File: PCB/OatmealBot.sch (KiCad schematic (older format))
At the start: 7 parts, among them J2 RPi_GPIO

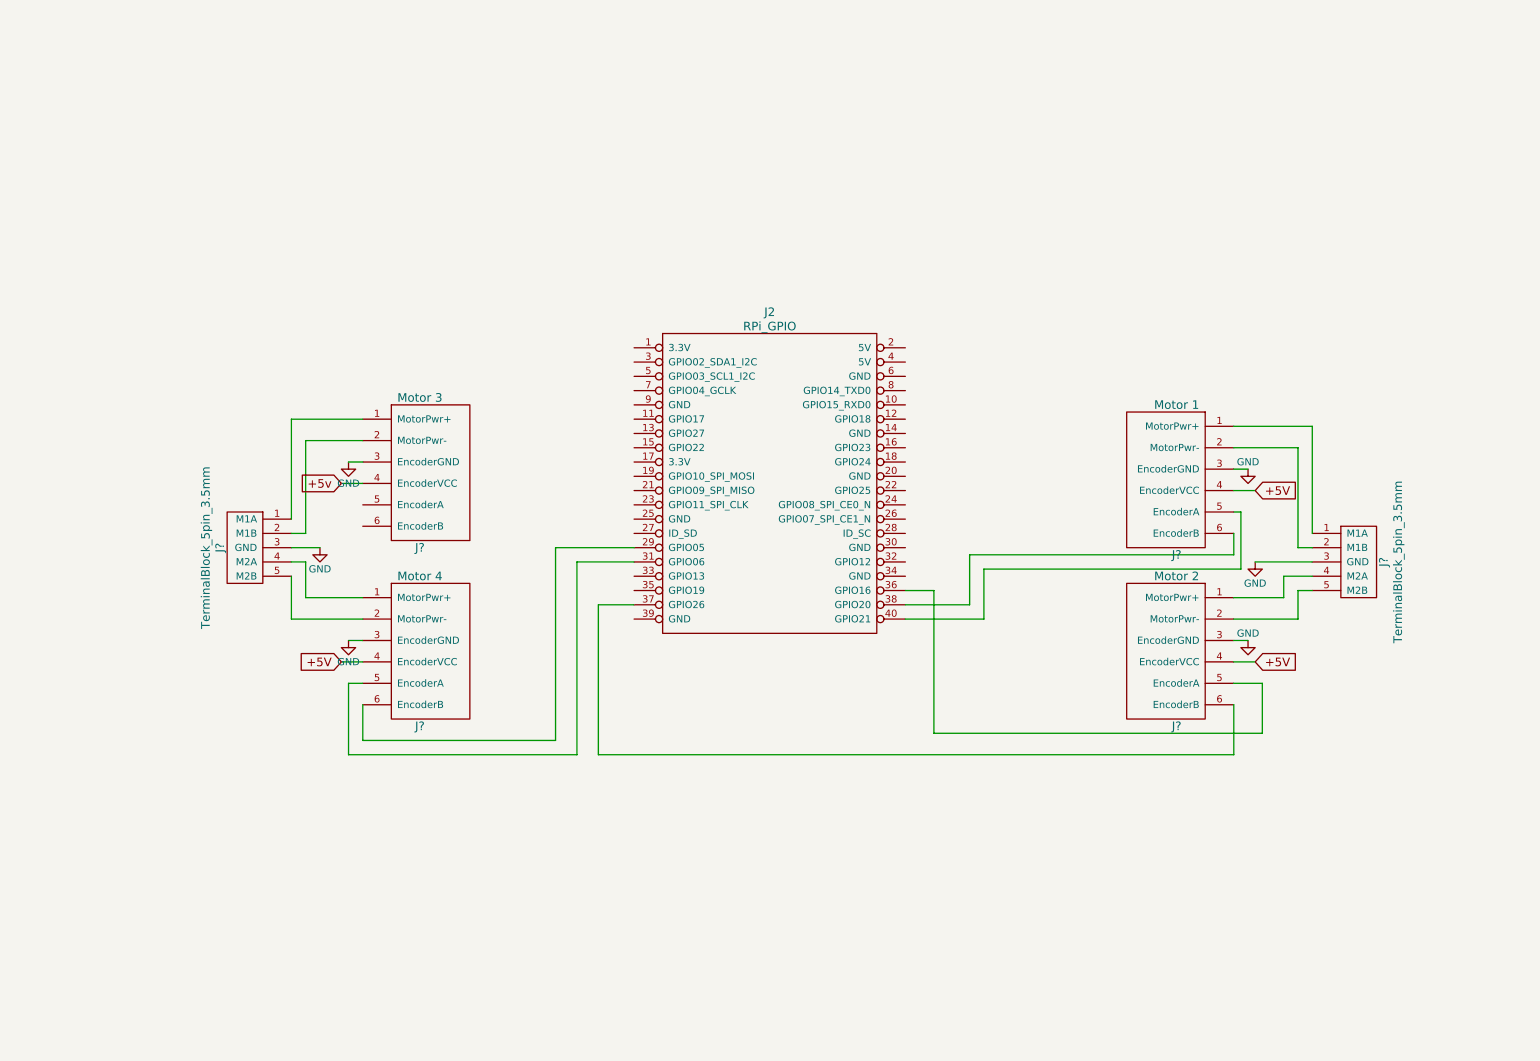
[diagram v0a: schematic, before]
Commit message: Added 5V to 3.3V level shifter on the encoder outputs. Hooked up all encoder outputs.
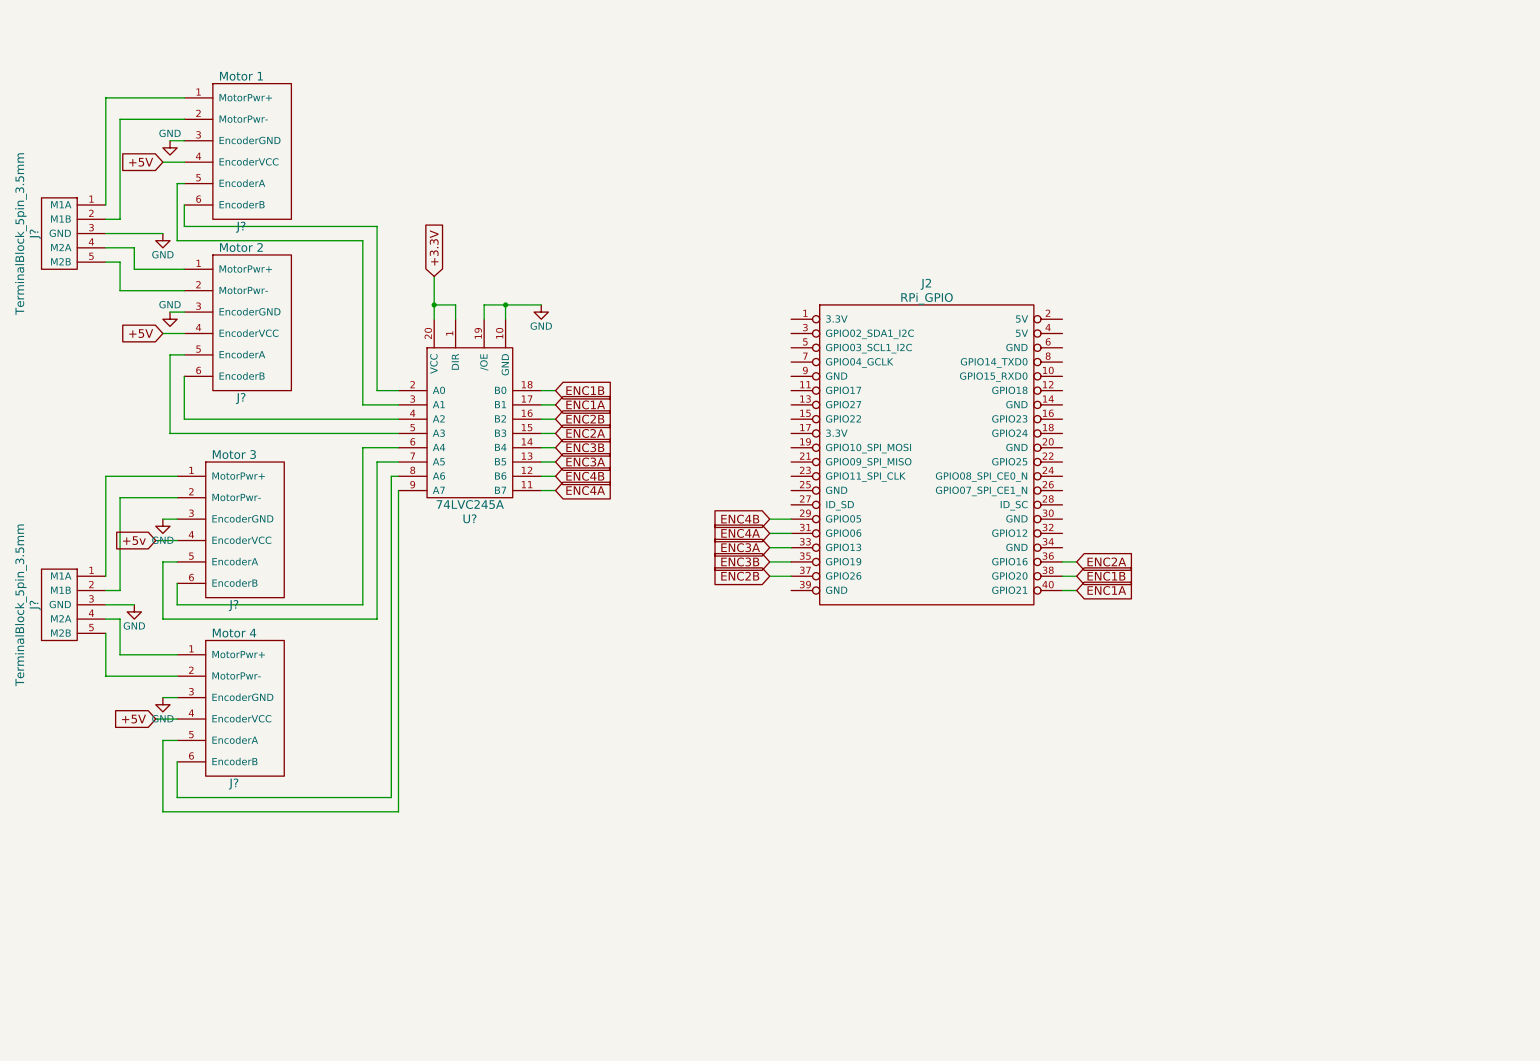
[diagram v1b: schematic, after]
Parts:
- added U?: 74LVC245A, symbol 74LVC245A
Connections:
- net GND: now also U?.10 (GND), U?.19 (/OE)
- net at J?.6 (EncoderB): now also U?.8 (A6); no longer J2.29 (GPIO05)
- net at J?.5 (EncoderA): now also U?.9 (A7); no longer J2.31 (GPIO06)
- net ENC3A: now reaches J2.33 (GPIO13)
- net ENC3A: now also U?.13 (B5)
- net ENC3B: now reaches J2.35 (GPIO19)
- net ENC3B: now also U?.14 (B4)
- net at J?.5 (EncoderA): now also U?.5 (A3); no longer J2.36 (GPIO16)
- net at J?.6 (EncoderB): now also U?.4 (A2); no longer J2.37 (GPIO26)
- net at J?.6 (EncoderB): now also U?.2 (A0); no longer J2.38 (GPIO20)
- net at J?.5 (EncoderA): now also U?.3 (A1); no longer J2.40 (GPIO21)
- net at J?.5 (EncoderA): now also U?.7 (A5)
- net at J?.6 (EncoderB): now also U?.6 (A4)
- new net +3.3V: U?.1 (DIR), U?.20 (VCC)
- new net ENC1A: J2.40 (GPIO21), U?.17 (B1)
- new net ENC1B: J2.38 (GPIO20), U?.18 (B0)
- new net ENC2A: J2.36 (GPIO16), U?.15 (B3)
- new net ENC2B: J2.37 (GPIO26), U?.16 (B2)
- new net ENC4A: J2.31 (GPIO06), U?.11 (B7)
- new net ENC4B: J2.29 (GPIO05), U?.12 (B6)
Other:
- moved on the sheet: J2, J?

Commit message: Added LEDs and servo connectors
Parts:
- added D? (x2): LED, symbol LED
- added J?: ServoHeader1, symbol ServoHeader
- added J?: ServoHeader2, symbol ServoHeader
- added J?: ServoHeader3, symbol ServoHeader
- added R? (x2): 330, symbol R
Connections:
- net +5V: now also J?.2 (Vcc), J?.2 (Vcc), J?.2 (Vcc)
- net GND: now also D?.1 (K), D?.1 (K), J?.1 (GND), J?.1 (GND), J?.1 (GND)
- net at J2.15 (GPIO22): now also R?.1
- net at J2.16 (GPIO23): now also R?.2
- new net: D?.2 (A), R?.1
- new net: D?.2 (A), R?.2
- new net Servo1: J?.3 (Signal)
- new net Servo2: J?.3 (Signal)
- new net Servo3: J?.3 (Signal)
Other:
- note added: "Verify Value"
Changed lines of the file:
@@
 Wire Wire Line
 	7900 4550 8000 4550
+$Comp
+L R R?
+U 1 1 5B24C1E3
+P 8350 3350
+F 0 "R?" V 8430 3350 50  0000 C CNN
+F 1 "330" V 8350 3350 50  0000 C CNN
+F 2 "" V 8280 3350 50  0000 C CNN
+F 3 "" H 8350 3350 50  0000 C CNN
+	1    8350 3350
+	0    1    1    0
+$EndComp
+$Comp
+L R R?
+U 1 1 5B24C256
+P 5700 3350
+F 0 "R?" V 5780 3350 50  0000 C CNN
+F 1 "330" V 5700 3350 50  0000 C CNN
+F 2 "" V 5630 3350 50  0000 C CNN
+F 3 "" H 5700 3350 50  0000 C CNN
+	1    5700 3350
+	0    1    1    0
+$EndComp
+$Comp
+L LED D?
+U 1 1 5B24C2BD
+P 8800 3350
+F 0 "D?" H 8800 3450 50  0000 C CNN
+F 1 "LED" H 8800 3250 50  0000 C CNN
+F 2 "" H 8800 3350 50  0000 C CNN
+F 3 "" H 8800 3350 50  0000 C CNN
+	1    8800 3350
+	-1   0    0    1
+$EndComp
+$Comp
+L LED D?
+U 1 1 5B24C3DB
+P 5250 3350
+F 0 "D?" H 5250 3450 50  0000 C CNN
+F 1 "LED" H 5250 3250 50  0000 C CNN
+F 2 "" H 5250 3350 50  0000 C CNN
+F 3 "" H 5250 3350 50  0000 C CNN
+	1    5250 3350
+	1    0    0    -1
+$EndComp
+$Comp
+L GND #PWR?
+U 1 1 5B24C448
+P 9200 3350
+F 0 "#PWR?" H 9200 3100 50  0001 C CNN
+F 1 "GND" H 9200 3200 50  0000 C CNN
+F 2 "" H 9200 3350 50  0000 C CNN
+F 3 "" H 9200 3350 50  0000 C CNN
+	1    9200 3350
+	1    0    0    -1
+$EndComp
+$Comp
+L GND #PWR?
+U 1 1 5B24C48C
+P 4900 3350
+F 0 "#PWR?" H 4900 3100 50  0001 C CNN
+F 1 "GND" H 4900 3200 50  0000 C CNN
+F 2 "" H 4900 3350 50  0000 C CNN
+F 3 "" H 4900 3350 50  0000 C CNN
+	1    4900 3350
+	1    0    0    -1
+$EndComp
+Wire Wire Line
+	7900 3350 8200 3350
+Wire Wire Line
+	8500 3350 8600 3350
+Wire Wire Line
+	9000 3350 9200 3350
+Wire Wire Line
+	6000 3350 5850 3350
+Wire Wire Line
+	5550 3350 5450 3350
+Wire Wire Line
+	5050 3350 4900 3350
+Text Notes 8600 3300 2    60   Italic 0
+Verify Value
+$Comp
+L ServoHeader J?
+U 1 1 5B24CC4B
+P 1250 7350
+F 0 "J?" V 1600 7200 60  0000 C CNN
+F 1 "ServoHeader1" H 1250 7000 60  0000 C CNN
+F 2 "" H 1200 7350 60  0001 C CNN
+F 3 "" H 1200 7350 60  0001 C CNN
+	1    1250 7350
+	1    0    0    -1
+$EndComp
+$Comp
+L ServoHeader J?
+U 1 1 5B24CCA8
+P 2100 7350
+F 0 "J?" V 2450 7200 60  0000 C CNN
+F 1 "ServoHeader2" H 2100 7000 60  0000 C CNN
+F 2 "" H 2050 7350 60  0001 C CNN
+F 3 "" H 2050 7350 60  0001 C CNN
+	1    2100 7350
+	1    0    0    -1
+$EndComp
+$Comp
+L ServoHeader J?
+U 1 1 5B24CCF1
+P 2950 7350
+F 0 "J?" V 3300 7200 60  0000 C CNN
+F 1 "ServoHeader3" H 2950 7000 60  0000 C CNN
+F 2 "" H 2900 7350 60  0001 C CNN
+F 3 "" H 2900 7350 60  0001 C CNN
+	1    2950 7350
+	1    0    0    -1
+$EndComp
+$Comp
+L GND #PWR?
+U 1 1 5B24CDE6
+P 800 6550
+F 0 "#PWR?" H 800 6300 50  0001 C CNN
+F 1 "GND" H 800 6400 50  0000 C CNN
+F 2 "" H 800 6550 50  0000 C CNN
+F 3 "" H 800 6550 50  0000 C CNN
+	1    800  6550
+	1    0    0    -1
+$EndComp
+Wire Wire Line
+	1050 7150 1050 6550
+Wire Wire Line
+	800  6550 2750 6550
+Wire Wire Line
+	1900 6550 1900 7150
+Connection ~ 1050 6550
+Wire Wire Line
+	2750 6550 2750 7150
+Connection ~ 1900 6550
+Text GLabel 800  6150 1    60   Input ~ 0
++5V
+Wire Wire Line
+	1250 7150 1250 6400
+Wire Wire Line
+	800  6400 2950 6400
+Wire Wire Line
+	800  6400 800  6150
+Wire Wire Line
+	2100 6400 2100 7150
+Connection ~ 1250 6400
+Wire Wire Line
+	2950 6400 2950 7150
+Connection ~ 2100 6400
+Text GLabel 1450 7000 1    60   Input Italic 0
+Servo1
+Text GLabel 2300 7000 1    60   Input Italic 0
+Servo2
+Text GLabel 3150 7000 1    60   Input Italic 0
+Servo3
+Wire Wire Line
+	1450 7150 1450 7000
+Wire Wire Line
+	2300 7150 2300 7000
+Wire Wire Line
+	3150 7150 3150 7000
 $EndSCHEMATC

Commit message: Added power connectors
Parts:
- added P?: Motor Hat Power, symbol CONN_01X02
- added U?: PololuD24V22F, symbol PololuD24V22F
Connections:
- net +5V: now also U?.5 (VOUT)
- net GND: now also P?.1 (P1), U?.4 (GND)
- new net +12V: P?.2 (P2), U?.3 (VIN)
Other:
- note added: "Add voltage protector on +5V!"
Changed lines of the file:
@@
 Wire Wire Line
 	3150 7150 3150 7000
+$Comp
+L PololuD24V22F U?
+U 1 1 5B288608
+P 10100 1000
+F 0 "U?" H 10250 1300 60  0000 C CNN
+F 1 "PololuD24V22F" H 10150 700 60  0000 C CNN
+F 2 "" H 9950 1100 60  0001 C CNN
+F 3 "" H 9950 1100 60  0001 C CNN
+	1    10100 1000
+	-1   0    0    1
+$EndComp
+$Comp
+L GND #PWR?
+U 1 1 5B28887D
+P 10500 900
+F 0 "#PWR?" H 10500 650 50  0001 C CNN
+F 1 "GND" H 10500 750 50  0000 C CNN
+F 2 "" H 10500 900 50  0000 C CNN
+F 3 "" H 10500 900 50  0000 C CNN
+	1    10500 900
+	1    0    0    -1
+$EndComp
+Text GLabel 10400 800  2    60   Input ~ 0
++5V
+Wire Wire Line
+	10300 800  10400 800
+Wire Wire Line
+	10300 900  10500 900
+$Comp
+L CONN_01X02 P?
+U 1 1 5B289648
+P 10000 1600
+F 0 "P?" H 10000 1750 50  0000 C CNN
+F 1 "Motor Hat Power" H 10200 1450 50  0000 C CNN
+F 2 "" H 10000 1600 50  0000 C CNN
+F 3 "" H 10000 1600 50  0000 C CNN
+	1    10000 1600
+	-1   0    0    1
+$EndComp
+$Comp
+L GND #PWR?
+U 1 1 5B2897C9
+P 10300 1650
+F 0 "#PWR?" H 10300 1400 50  0001 C CNN
+F 1 "GND" H 10300 1500 50  0000 C CNN
+F 2 "" H 10300 1650 50  0000 C CNN
+F 3 "" H 10300 1650 50  0000 C CNN
+	1    10300 1650
+	1    0    0    -1
+$EndComp
+$Comp
+L +12V #PWR?
+U 1 1 5B289821
+P 10300 1550
+F 0 "#PWR?" H 10300 1400 50  0001 C CNN
+F 1 "+12V" H 10300 1690 50  0000 C CNN
+F 2 "" H 10300 1550 50  0000 C CNN
+F 3 "" H 10300 1550 50  0000 C CNN
+	1    10300 1550
+	1    0    0    -1
+$EndComp
+Wire Wire Line
+	10200 1550 10300 1550
+Wire Wire Line
+	10200 1650 10300 1650
+$Comp
+L +12V #PWR?
+U 1 1 5B289B43
+P 10750 1000
+F 0 "#PWR?" H 10750 850 50  0001 C CNN
+F 1 "+12V" H 10750 1150 50  0000 C CNN
+F 2 "" H 10750 1000 50  0000 C CNN
+F 3 "" H 10750 1000 50  0000 C CNN
+	1    10750 1000
+	1    0    0    -1
+$EndComp
+Wire Wire Line
+	10300 1000 10750 1000
+Text Notes 9300 600  0    60   ~ 0
+Add voltage protector on +5V!
 $EndSCHEMATC

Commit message: Added serial port connector
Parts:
- added R? (x2): R, symbol R
- added U?: FTDI-Cable, symbol FTDI-Cable
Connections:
- net GND: now also R?.2, U?.1 (GND)
- net PI_RXD: now reaches J2.10 (GPIO15_RXD0)
- net PI_RXD: now also R?.1, R?.2
- net PI_TXD: now reaches J2.8 (GPIO14_TXD0)
- net PI_TXD: now also U?.5 (RXD)
- new net: R?.1, U?.4 (TXD)
- no-connect marks 0 -> 3
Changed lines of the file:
@@
 Text Notes 9300 600  0    60   ~ 0
 Add voltage protector on +5V!
+$Comp
+L FTDI-Cable U?
+U 1 1 5B299B43
+P 9700 5600
+F 0 "U?" H 9850 5200 60  0000 C CNN
+F 1 "FTDI-Cable" V 10050 5550 60  0000 C CNN
+F 2 "" H 9700 5500 60  0001 C CNN
+F 3 "" H 9700 5500 60  0001 C CNN
+	1    9700 5600
+	-1   0    0    1
+$EndComp
+$Comp
+L GND #PWR?
+U 1 1 5B299D08
+P 10000 5800
+F 0 "#PWR?" H 10000 5550 50  0001 C CNN
+F 1 "GND" H 10000 5650 50  0000 C CNN
+F 2 "" H 10000 5800 50  0000 C CNN
+F 3 "" H 10000 5800 50  0000 C CNN
+	1    10000 5800
+	1    0    0    -1
+$EndComp
+NoConn ~ 9900 5600
+NoConn ~ 9900 5700
+NoConn ~ 9900 5300
+Text GLabel 10000 5400 2    60   Output ~ 0
+PI_TXD
+Text GLabel 8000 2950 2    60   Output ~ 0
+PI_TXD
+Text GLabel 8400 3050 2    60   Input ~ 0
+PI_RXD
+Text GLabel 10650 5900 2    60   Input ~ 0
+PI_RXD
+$Comp
+L R R?
+U 1 1 5B29AE0F
+P 10550 5650
+F 0 "R?" V 10630 5650 50  0000 C CNN
+F 1 "R" V 10550 5650 50  0000 C CNN
+F 2 "" V 10480 5650 50  0000 C CNN
+F 3 "" H 10550 5650 50  0000 C CNN
+	1    10550 5650
+	1    0    0    -1
+$EndComp
+$Comp
+L R R?
+U 1 1 5B29AECC
+P 10550 6150
+F 0 "R?" V 10630 6150 50  0000 C CNN
+F 1 "R" V 10550 6150 50  0000 C CNN
+F 2 "" V 10480 6150 50  0000 C CNN
+F 3 "" H 10550 6150 50  0000 C CNN
+	1    10550 6150
+	1    0    0    -1
+$EndComp
+$Comp
+L GND #PWR?
+U 1 1 5B29AF0F
+P 10550 6350
+F 0 "#PWR?" H 10550 6100 50  0001 C CNN
+F 1 "GND" H 10550 6200 50  0000 C CNN
+F 2 "" H 10550 6350 50  0000 C CNN
+F 3 "" H 10550 6350 50  0000 C CNN
+	1    10550 6350
+	1    0    0    -1
+$EndComp
+Wire Wire Line
+	10550 6350 10550 6300
+Wire Wire Line
+	10550 6000 10550 5800
+Wire Wire Line
+	10550 5500 9900 5500
+Wire Wire Line
+	10650 5900 10550 5900
+Connection ~ 10550 5900
+Wire Wire Line
+	7900 2950 8000 2950
+Wire Wire Line
+	8400 3050 7900 3050
+Wire Wire Line
+	9900 5400 10000 5400
+Wire Wire Line
+	9900 5800 10000 5800
 $EndSCHEMATC

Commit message: Added OLED SPI connector
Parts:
- added U?: SPI_OLED, symbol SPI_OLED
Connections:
- net GND: now also U?.1 (GND)
- net OLED_RESET: now reaches J2.18 (GPIO24)
- net OLED_RESET: now also U?.5 (Reset)
- net MOSI: now reaches J2.19 (GPIO10_SPI_MOSI)
- net MOSI: now also U?.4 (MOSI)
- net MISO: now reaches J2.21 (GPIO09_SPI_MISO)
- net OLED_DC: now reaches J2.22 (GPIO25)
- net OLED_DC: now also U?.6 (DC)
- net SCLK: now reaches J2.23 (GPIO11_SPI_CLK)
- net SCLK: now also U?.3 (CLK)
- net OLED_CS: now reaches J2.24 (GPIO08_SPI_CE0_N)
- net OLED_CS: now also U?.7 (CS)
- new net +3V3: U?.2 (VCC)
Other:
- moved on the sheet: D?, R?
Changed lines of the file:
@@
 L R R?
 U 1 1 5B24C1E3
-P 8350 3350
-F 0 "R?" V 8430 3350 50  0000 C CNN
-F 1 "330" V 8350 3350 50  0000 C CNN
-F 2 "" V 8280 3350 50  0000 C CNN
-F 3 "" H 8350 3350 50  0000 C CNN
-	1    8350 3350
+P 8750 3350
+F 0 "R?" V 8830 3350 50  0000 C CNN
+F 1 "330" V 8750 3350 50  0000 C CNN
+F 2 "" V 8680 3350 50  0000 C CNN
+F 3 "" H 8750 3350 50  0000 C CNN
+	1    8750 3350
 	0    1    1    0
 $EndComp
@@
 L LED D?
 U 1 1 5B24C2BD
-P 8800 3350
-F 0 "D?" H 8800 3450 50  0000 C CNN
-F 1 "LED" H 8800 3250 50  0000 C CNN
-F 2 "" H 8800 3350 50  0000 C CNN
-F 3 "" H 8800 3350 50  0000 C CNN
-	1    8800 3350
+P 9200 3350
+F 0 "D?" H 9200 3450 50  0000 C CNN
+F 1 "LED" H 9200 3250 50  0000 C CNN
+F 2 "" H 9200 3350 50  0000 C CNN
+F 3 "" H 9200 3350 50  0000 C CNN
+	1    9200 3350
 	-1   0    0    1
 $EndComp
@@
 L GND #PWR?
 U 1 1 5B24C448
-P 9200 3350
-F 0 "#PWR?" H 9200 3100 50  0001 C CNN
-F 1 "GND" H 9200 3200 50  0000 C CNN
-F 2 "" H 9200 3350 50  0000 C CNN
-F 3 "" H 9200 3350 50  0000 C CNN
-	1    9200 3350
+P 9600 3350
+F 0 "#PWR?" H 9600 3100 50  0001 C CNN
+F 1 "GND" H 9600 3200 50  0000 C CNN
+F 2 "" H 9600 3350 50  0000 C CNN
+F 3 "" H 9600 3350 50  0000 C CNN
+	1    9600 3350
 	1    0    0    -1
 $EndComp
@@
 $EndComp
 Wire Wire Line
-	7900 3350 8200 3350
-Wire Wire Line
-	8500 3350 8600 3350
-Wire Wire Line
-	9000 3350 9200 3350
+	7900 3350 8600 3350
+Wire Wire Line
+	8900 3350 9000 3350
+Wire Wire Line
+	9400 3350 9600 3350
 Wire Wire Line
 	6000 3350 5850 3350
@@
 Wire Wire Line
 	5050 3350 4900 3350
-Text Notes 8600 3300 2    60   Italic 0
+Text Notes 9000 3300 2    60   Italic 0
 Verify Value
 $Comp
@@
 	10550 6350 10550 6300
 Wire Wire Line
-	10550 6000 10550 5800
+	10550 5800 10550 6000
 Wire Wire Line
 	10550 5500 9900 5500
@@
 Wire Wire Line
 	9900 5800 10000 5800
+$Comp
+L SPI_OLED U?
+U 1 1 5B29A40B
+P 6900 5750
+F 0 "U?" V 7300 5650 60  0000 C CNN
+F 1 "SPI_OLED" H 6900 5450 60  0000 C CNN
+F 2 "" H 6800 5750 60  0001 C CNN
+F 3 "" H 6800 5750 60  0001 C CNN
+	1    6900 5750
+	0    -1   -1   0
+$EndComp
+$Comp
+L GND #PWR?
+U 1 1 5B29A611
+P 6550 6050
+F 0 "#PWR?" H 6550 5800 50  0001 C CNN
+F 1 "GND" H 6550 5900 50  0000 C CNN
+F 2 "" H 6550 6050 50  0000 C CNN
+F 3 "" H 6550 6050 50  0000 C CNN
+	1    6550 6050
+	1    0    0    -1
+$EndComp
+$Comp
+L +3.3V #PWR?
+U 1 1 5B29B07B
+P 6150 5950
+F 0 "#PWR?" H 6150 5800 50  0001 C CNN
+F 1 "+3.3V" H 6150 6090 50  0000 C CNN
+F 2 "" H 6150 5950 50  0000 C CNN
+F 3 "" H 6150 5950 50  0000 C CNN
+	1    6150 5950
+	1    0    0    -1
+$EndComp
+Wire Wire Line
+	6700 6050 6550 6050
+Wire Wire Line
+	6700 5950 6150 5950
+Text GLabel 6600 5850 0    60   Input ~ 0
+SCLK
+Text GLabel 5850 3750 0    60   Output ~ 0
+SCLK
+Wire Wire Line
+	6000 3750 5850 3750
+Wire Wire Line
+	6700 5850 6600 5850
+Text GLabel 5850 3550 0    60   Output ~ 0
+MOSI
+Text GLabel 6600 5750 0    60   Input ~ 0
+MOSI
+Text GLabel 6600 5650 0    60   Input ~ 0
+OLED_RESET
+Text GLabel 6600 5550 0    60   Input ~ 0
+OLED_DC
+Text GLabel 6600 5450 0    60   Input ~ 0
+OLED_CS
+Wire Wire Line
+	6700 5750 6600 5750
+Wire Wire Line
+	6700 5650 6600 5650
+Wire Wire Line
+	6700 5550 6600 5550
+Wire Wire Line
+	6700 5450 6600 5450
+Text GLabel 5850 3650 0    60   Output ~ 0
+MISO
+Wire Wire Line
+	6000 3650 5850 3650
+Wire Wire Line
+	6000 3550 5850 3550
+Text GLabel 8000 3450 2    60   Output ~ 0
+OLED_RESET
+Wire Wire Line
+	8000 3450 7900 3450
+Text GLabel 8000 3650 2    60   Output ~ 0
+OLED_DC
+Wire Wire Line
+	8000 3650 7900 3650
+Text GLabel 8000 3750 2    60   Output ~ 0
+OLED_CS
+Wire Wire Line
+	8000 3750 7900 3750
 $EndSCHEMATC

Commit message: Hooked up the servo outputs correctly. Fixed a lot of design rule problems.
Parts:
- J5, J6, J8: renamed from J?; footprint (none) -> Pin_Headers:Pin_Header_Straight_1x06_Pitch2.54mm
- J9: renamed from J?; footprint (none) -> Pin_Headers:Pin_Header_Angled_1x06_Pitch2.54mm
- gave numbers to parts that had none: 16
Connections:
- net +5v is gone; now on net +5V: J5.4 (EncoderVCC)
- net +3.3V: now also J2.1 (3.3V)
- net +5V: now also J2.2 (5V), J2.4 (5V)
- net GND: now also J2.14 (GND), J2.20 (GND), J2.25 (GND), J2.30 (GND), J2.34 (GND), J2.39 (GND), J2.6 (GND), J2.9 (GND)
- net Servo1: now also J2.32 (GPIO12)
- net Servo2: now also J2.12 (GPIO18)
- net Servo3: now also J2.11 (GPIO17)
- no-connect marks 3 -> 5

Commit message: Started assigning some footprints. Initial PCB layout.
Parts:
- J9: footprint Pin_Headers:Pin_Header_Angled_1x06_Pitch2.54mm -> Pin_Headers:Pin_Header_Straight_1x06_Pitch2.54mm
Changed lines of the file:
@@
 F 0 "J9" H 2150 2100 60  0000 C CNN
 F 1 "Motor 2" H 2150 3150 60  0000 C CNN
-F 2 "Pin_Headers:Pin_Header_Angled_1x06_Pitch2.54mm" H 2250 2450 60  0001 C CNN
+F 2 "Pin_Headers:Pin_Header_Straight_1x06_Pitch2.54mm" H 2250 2450 60  0001 C CNN
 F 3 "" H 2250 2450 60  0001 C CNN
 	1    2150 2650
